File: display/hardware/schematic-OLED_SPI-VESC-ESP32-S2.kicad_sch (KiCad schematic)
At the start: 6 parts

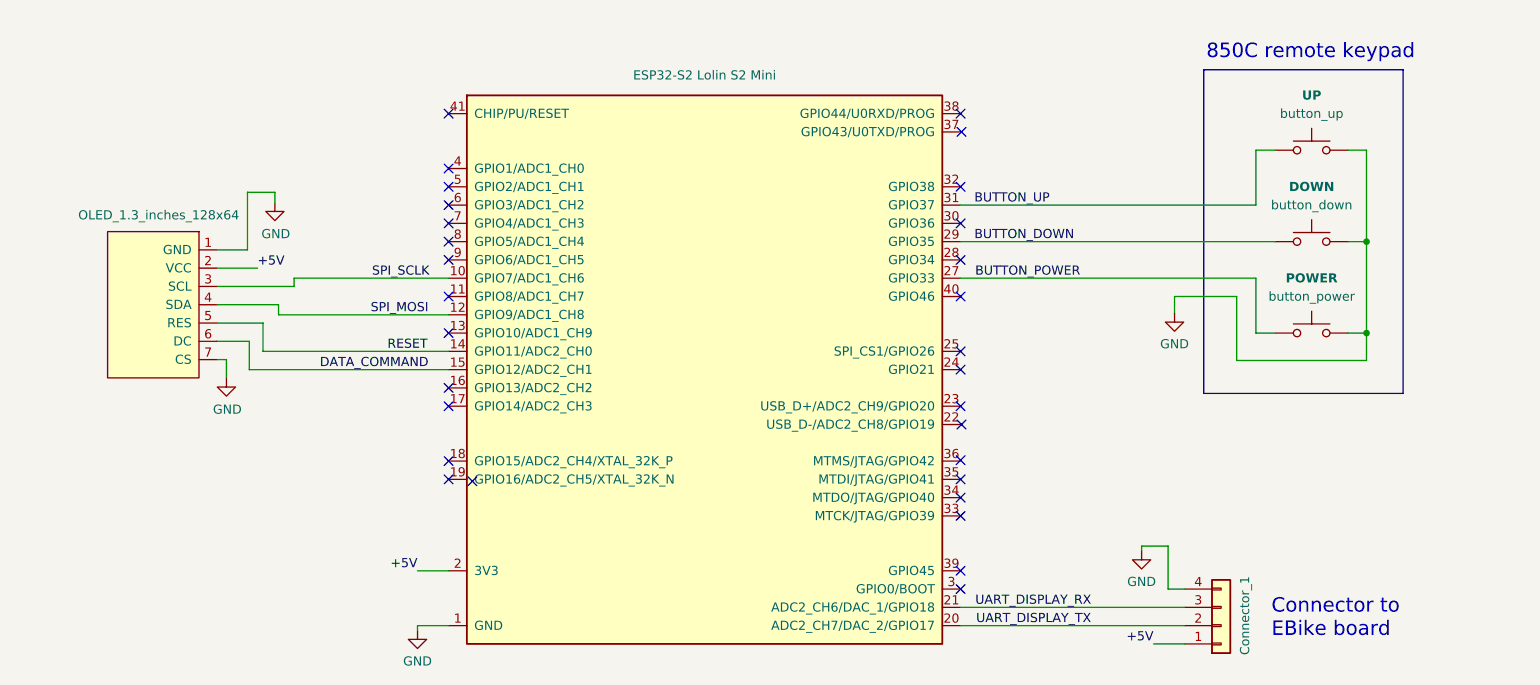
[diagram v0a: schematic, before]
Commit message: Updated the schematics by removing the UART connection between the EBike board and the display
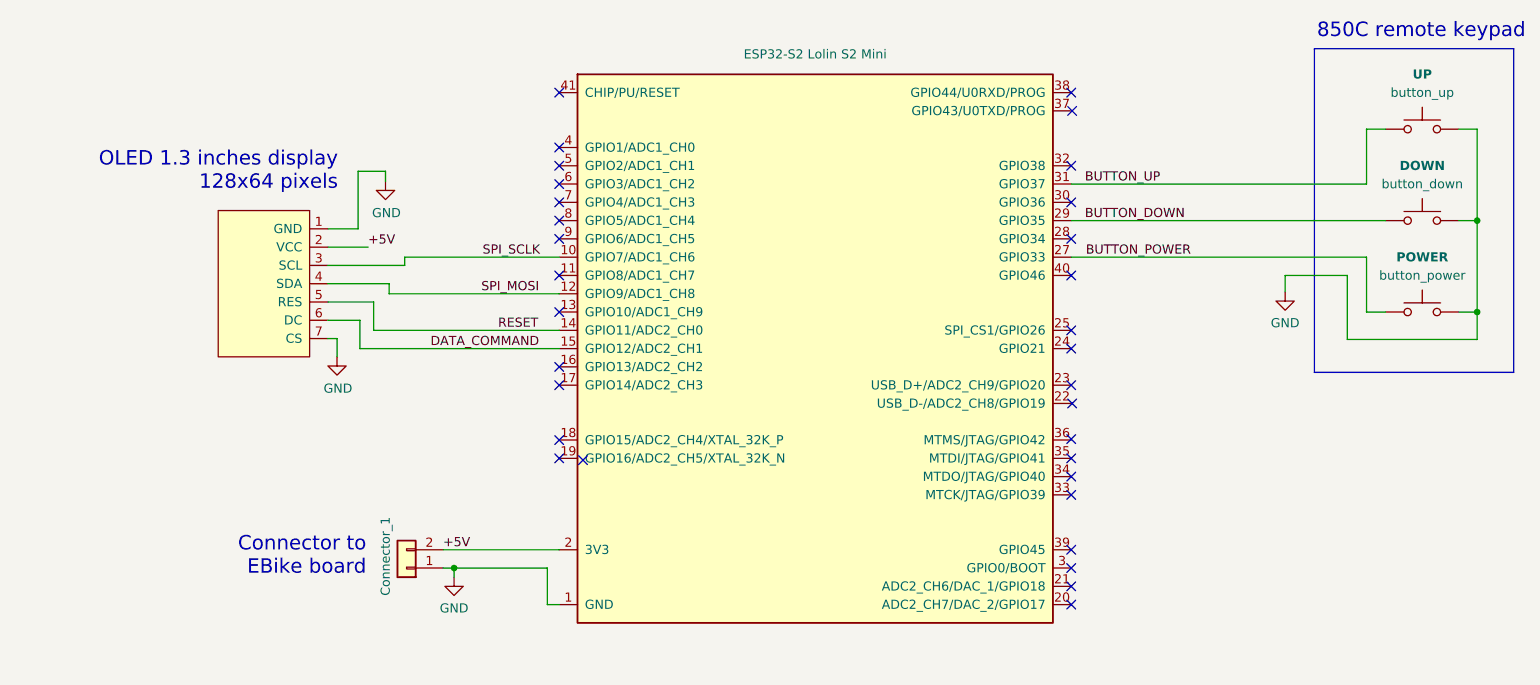
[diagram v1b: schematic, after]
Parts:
- removed J?: Connector_1, symbol Connector_Generic:Conn_01x04
- added J2: Connector_1, symbol Connector_Generic:Conn_01x02
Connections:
- net +5V: now also J2.2 (Pin_2)
- net GND: now also J2.1 (Pin_1)
- net UART_DISPLAY_RX: no longer names the net of U?.21 (ADC2_CH6/DAC_1/GPIO18)
- net UART_DISPLAY_TX: no longer names the net of U?.20 (ADC2_CH7/DAC_2/GPIO17)
- no-connect marks 30 -> 32
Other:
- note added: "OLED 1.3 inches display 128x64 pixels"
- moved on the sheet: button_down, button_power, button_up
